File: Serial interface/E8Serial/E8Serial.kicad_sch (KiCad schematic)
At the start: 51 parts, among them J1 Conn_01x04_Male, J2 Conn_01x04_Male, J3 Conn_01x04_Male, J4 Conn_01x04_Male, Q1 BC548, Q2 BC548, Q3 BC548, SW1 NDB2, SW2 NDB1, SW3 PARITY ODD_EVEN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

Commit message: Schematic update 2024-04-14 plus fixes
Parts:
- removed U8: 74LS123, Package_DIP:DIP-16_W7.62mm, symbol E8Serial-rescue:74LS123-74xx
- added U8: (no value), Package_DIP:DIP-16_W7.62mm_Socket_LongPads, symbol DM series IC:DM9602
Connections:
- net +5V: now also U8.16 (VCC)
- net GND: now also U8.11 (A), U8.5 (A), U8.8 (GND)
- net SL: now also U8.7 (~{Q})
- net ~{RDA}: now also U8.9 (~{Q})
- net at U4.21 (XR): now also U5.12
- net at C5.1, R13.1: now also U8.1 (Cext)
- net at C5.2: now also U8.2 (RCext)
- net at U5.2: now also U8.4 (B)
- net at C6.2: now also U8.14 (RCext)
- net at C6.1, R14.1: now also U8.15 (Cext)
- new net: U8.12 (B), U8.6 (Q)
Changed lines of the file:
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@@
     (pin "1")
-  )
-  (symbol (lib_id "E8Serial-rescue:74LS123-74xx") (at 208.28 205.74 0) (unit 1)
-    (in_bom yes) (on_board yes)
-    (property "Reference" "U8" (id 0) (at 208.28 193.8782 0))
-    (property "Value" "74LS123" (id 1) (at 208.28 196.1896 0))
-    (property "Footprint" "Package_DIP:DIP-16_W7.62mm" (id 2) (at 208.28 205.74 0)
-      (effects (font (size 1.27 1.27)) hide)
-    )
-    (property "Datasheet" "http://www.ti.com/lit/gpn/sn74LS123" (id 3) (at 208.28 205.74 0)
-      (effects (font (size 1.27 1.27)) hide)
-    )
-    (pin "1")
-    (pin "13")
-    (pin "14")
-    (pin "15")
-    (pin "2")
-    (pin "3")
-    (pin "4")
-    (pin "10")
-    (pin "11")
-    (pin "12")
-    (pin "5")
-    (pin "6")
-    (pin "7")
-    (pin "9")
-    (pin "16")
-    (pin "8")
-  )
-  (symbol (lib_id "E8Serial-rescue:74LS123-74xx") (at 251.46 205.74 0) (unit 2)
-    (in_bom yes) (on_board yes)
-    (property "Reference" "U8" (id 0) (at 251.46 193.8782 0))
-    (property "Value" "74LS123" (id 1) (at 251.46 196.1896 0))
-    (property "Footprint" "Package_DIP:DIP-16_W7.62mm" (id 2) (at 251.46 205.74 0)
-      (effects (font (size 1.27 1.27)) hide)
-    )
-    (property "Datasheet" "http://www.ti.com/lit/gpn/sn74LS123" (id 3) (at 251.46 205.74 0)
-      (effects (font (size 1.27 1.27)) hide)
-    )
-    (pin "1")
-    (pin "13")
-    (pin "14")
-    (pin "15")
-    (pin "2")
-    (pin "3")
-    (pin "4")
-    (pin "10")
-    (pin "11")
-    (pin "12")
-    (pin "5")
-    (pin "6")
-    (pin "7")
-    (pin "9")
-    (pin "16")
-    (pin "8")
   )
   (symbol (lib_id "Device:R") (at 234.95 184.15 0) (mirror x) (unit 1)
@@
     (pin "4")
   )
-  (symbol (lib_id "E8Serial-rescue:74LS123-74xx") (at 27.94 260.35 0) (unit 3)
-    (in_bom yes) (on_board yes)
-    (property "Reference" "U8" (id 0) (at 33.782 259.1816 0)
-      (effects (font (size 1.27 1.27)) (justify left))
-    )
-    (property "Value" "74LS123" (id 1) (at 33.782 261.493 0)
-      (effects (font (size 1.27 1.27)) (justify left))
-    )
-    (property "Footprint" "" (id 2) (at 27.94 260.35 0)
-      (effects (font (size 1.27 1.27)) hide)
-    )
-    (property "Datasheet" "http://www.ti.com/lit/gpn/sn74LS123" (id 3) (at 27.94 260.35 0)
-      (effects (font (size 1.27 1.27)) hide)
-    )
-    (pin "1")
-    (pin "13")
-    (pin "14")
-    (pin "15")
-    (pin "2")
-    (pin "3")
-    (pin "4")
-    (pin "10")
-    (pin "11")
-    (pin "12")
-    (pin "5")
-    (pin "6")
-    (pin "7")
-    (pin "9")
-    (pin "16")
-    (pin "8")
-  )
   (symbol (lib_id "74xx:74LS04") (at 55.88 260.35 0) (unit 7)
     (in_bom yes) (on_board yes)
@@
     (pin "1")
   )
+  (symbol (lib_name "DM9602_1") (lib_id "DM series IC:DM9602") (at 251.46 205.74 0) (unit 2)
+    (in_bom yes) (on_board yes) (fields_autoplaced)
+    (property "Reference" "U8" (id 0) (at 251.46 194.4202 0))
+    (property "Value" "" (id 1) (at 251.46 196.9571 0))
+    (property "Footprint" "Package_DIP:DIP-16_W7.62mm_Socket_LongPads" (id 2) (at 251.46 205.74 0)
+      (effects (font (size 1.27 1.27)) hide)
+    )
+    (property "Datasheet" "http://www.ti.com/lit/gpn/sn74LS123" (id 3) (at 251.46 205.74 0)
+      (effects (font (size 1.27 1.27)) hide)
+    )
+    (pin "1")
+    (pin "2")
+    (pin "3")
+    (pin "4")
+    (pin "5")
+    (pin "6")
+    (pin "7")
+    (pin "10")
+    (pin "11")
+    (pin "12")
+    (pin "13")
+    (pin "14")
+    (pin "15")
+    (pin "9")
+    (pin "16")
+    (pin "8")
+  )
+  (symbol (lib_id "DM series IC:DM9602") (at 208.28 205.74 0) (unit 1)
+    (in_bom yes) (on_board yes) (fields_autoplaced)
+    (property "Reference" "U8" (id 0) (at 208.28 194.4202 0))
+    (property "Value" "" (id 1) (at 208.28 196.9571 0))
+    (property "Footprint" "" (id 2) (at 208.28 205.74 0)
+      (effects (font (size 1.27 1.27)) hide)
+    )
+    (property "Datasheet" "http://www.ti.com/lit/gpn/sn74LS123" (id 3) (at 208.28 205.74 0)
+      (effects (font (size 1.27 1.27)) hide)
+    )
+    (pin "1")
+    (pin "2")
+    (pin "3")
+    (pin "4")
+    (pin "5")
+    (pin "6")
+    (pin "7")
+    (pin "10")
+    (pin "11")
+    (pin "12")
+    (pin "12")
+    (pin "13")
+    (pin "14")
+    (pin "15")
+    (pin "16")
+    (pin "8")
+  )
+  (symbol (lib_id "DM series IC:DM9602") (at 27.94 260.35 0) (unit 3)
+    (in_bom yes) (on_board yes) (fields_autoplaced)
+    (property "Reference" "U8" (id 0) (at 33.782 259.5153 0)
+      (effects (font (size 1.27 1.27)) (justify left))
+    )
+    (property "Value" "" (id 1) (at 33.782 262.0522 0)
+      (effects (font (size 1.27 1.27)) (justify left))
+    )
+    (property "Footprint" "" (id 2) (at 27.94 260.35 0)
+      (effects (font (size 1.27 1.27)) hide)
+    )
+    (property "Datasheet" "http://www.ti.com/lit/gpn/sn74LS123" (id 3) (at 27.94 260.35 0)
+      (effects (font (size 1.27 1.27)) hide)
+    )
+    (pin "1")
+    (pin "2")
+    (pin "3")
+    (pin "4")
+    (pin "5")
+    (pin "6")
+    (pin "7")
+    (pin "10")
+    (pin "11")
+    (pin "12")
+    (pin "12")
+    (pin "13")
+    (pin "14")
+    (pin "15")
+    (pin "16")
+    (pin "8")
+  )
   (sheet_instances
     (path "/" (page "1"))
@@
       (reference "U7") (unit 1) (value "74LS165") (footprint "Package_DIP:DIP-16_W7.62mm")
     )
-    (path "/00000000-0000-0000-0000-000060e2db07"
-      (reference "U8") (unit 1) (value "74LS123") (footprint "Package_DIP:DIP-16_W7.62mm")
-    )
-    (path "/00000000-0000-0000-0000-000060e2f004"
-      (reference "U8") (unit 2) (value "74LS123") (footprint "Package_DIP:DIP-16_W7.62mm")
-    )
-    (path "/00000000-0000-0000-0000-00006143e14e"
-      (reference "U8") (unit 3) (value "74LS123") (footprint "")
-    )
-  )
+    (path "/89b31927-f663-4a3a-a530-c0fd8571c8d7"
+      (reference "U8") (unit 1) (value "DM9602") (footprint "Package_DIP:DIP-16_W7.62mm_Socket_LongPads")
+    )
+    (path "/1961fd7e-ea48-4fcd-9643-319fdbe0bda8"
+      (reference "U8") (unit 2) (value "DM9602") (footprint "Package_DIP:DIP-16_W7.62mm_Socket_LongPads")
+    )
+    (path "/a3990e5d-c3b4-40a6-9c0e-38537b9470eb"
+      (reference "U8") (unit 3) (value "DM9602") (footprint "Package_DIP:DIP-16_W7.62mm_Socket_LongPads")
+    )
+  )

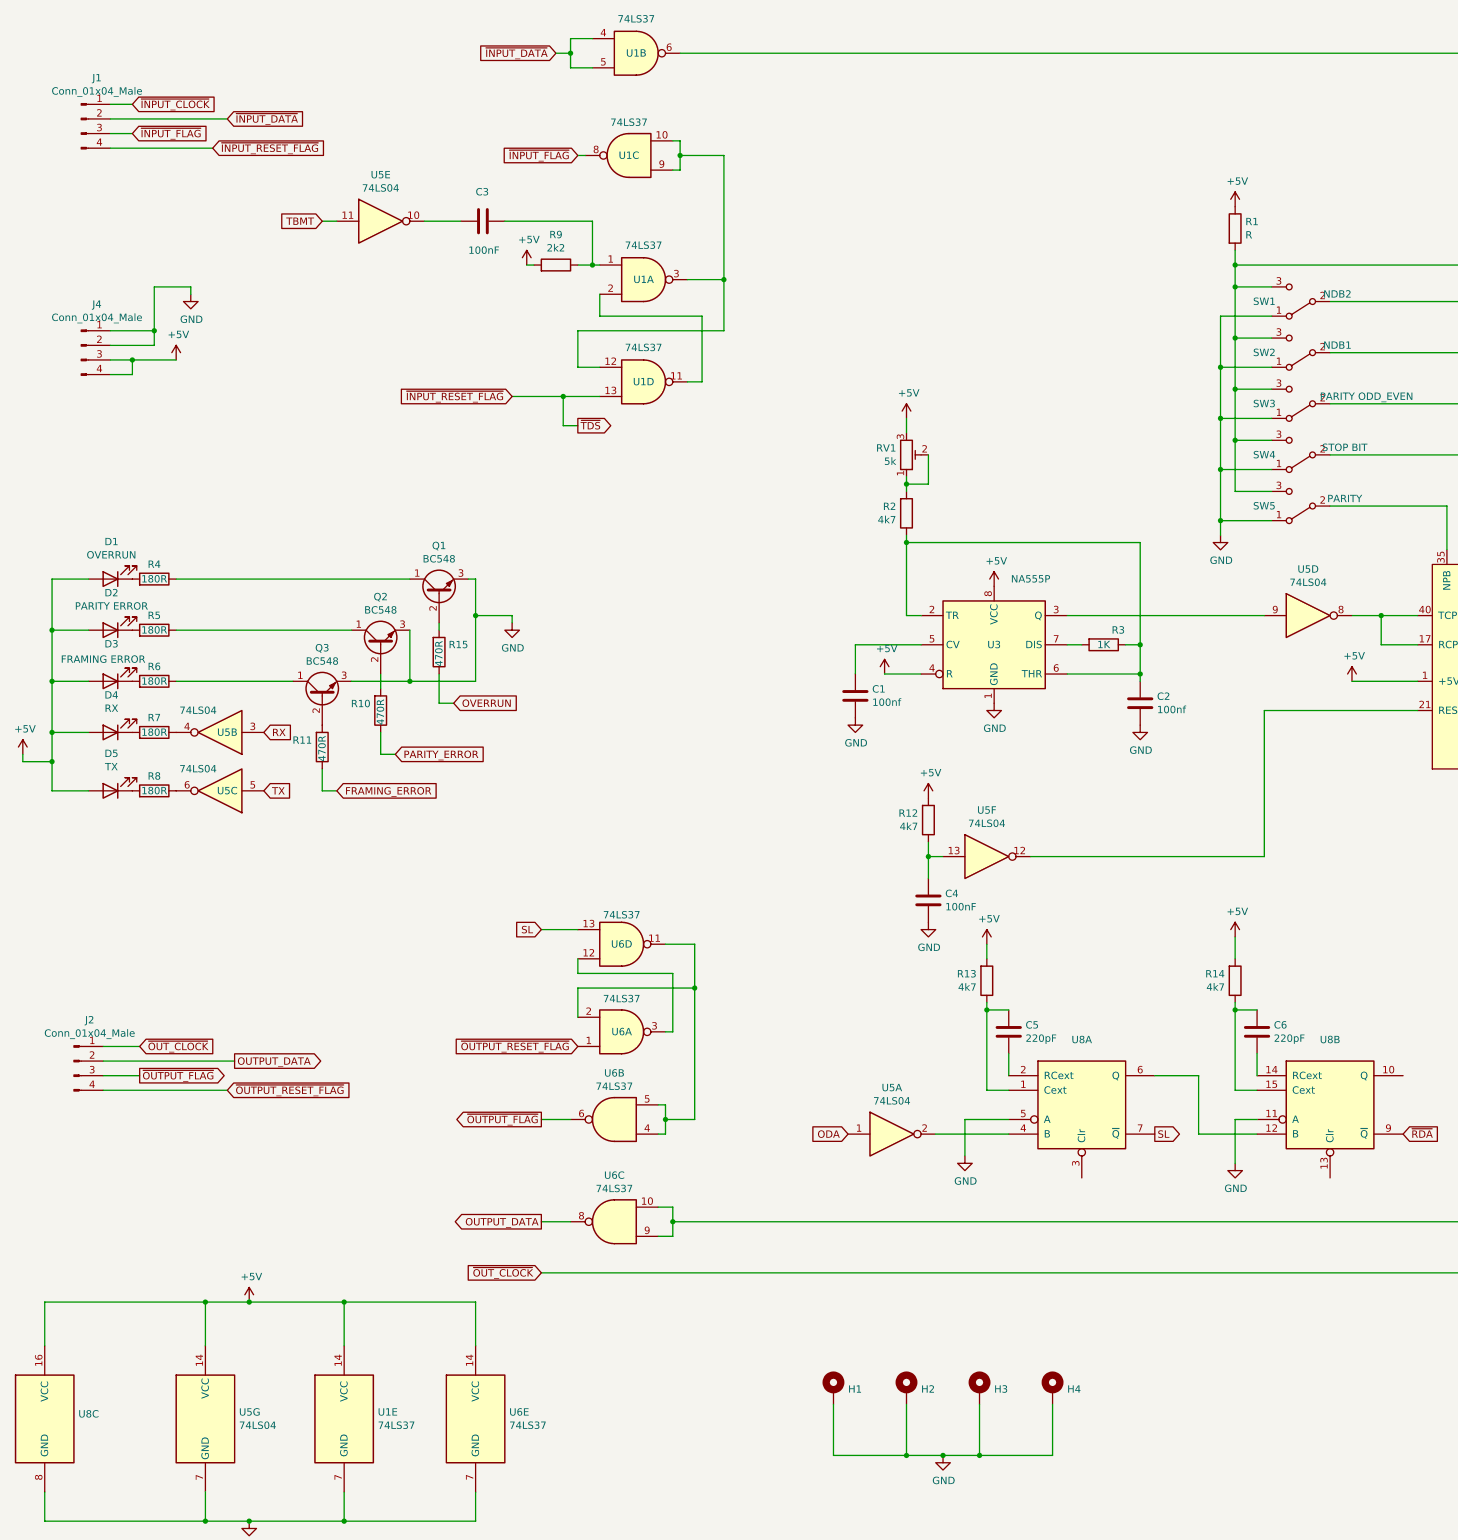
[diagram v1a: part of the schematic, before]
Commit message: Changes 20-7-2025 E8/T. Connected 3 missing supply rail tracks to ICS Added flood fill top and bottom to reduce noise E8/F Corrected labelling on RHS board to reflect EXT_LA not GND Changed fast slow switch operation so fast is in the DOWN position. E8/C. Ran a new track to the 2 pin JST connector from EXT_LA from 10 pin connector on SR input. Added files for E8MX, 2k byte memory expansion board
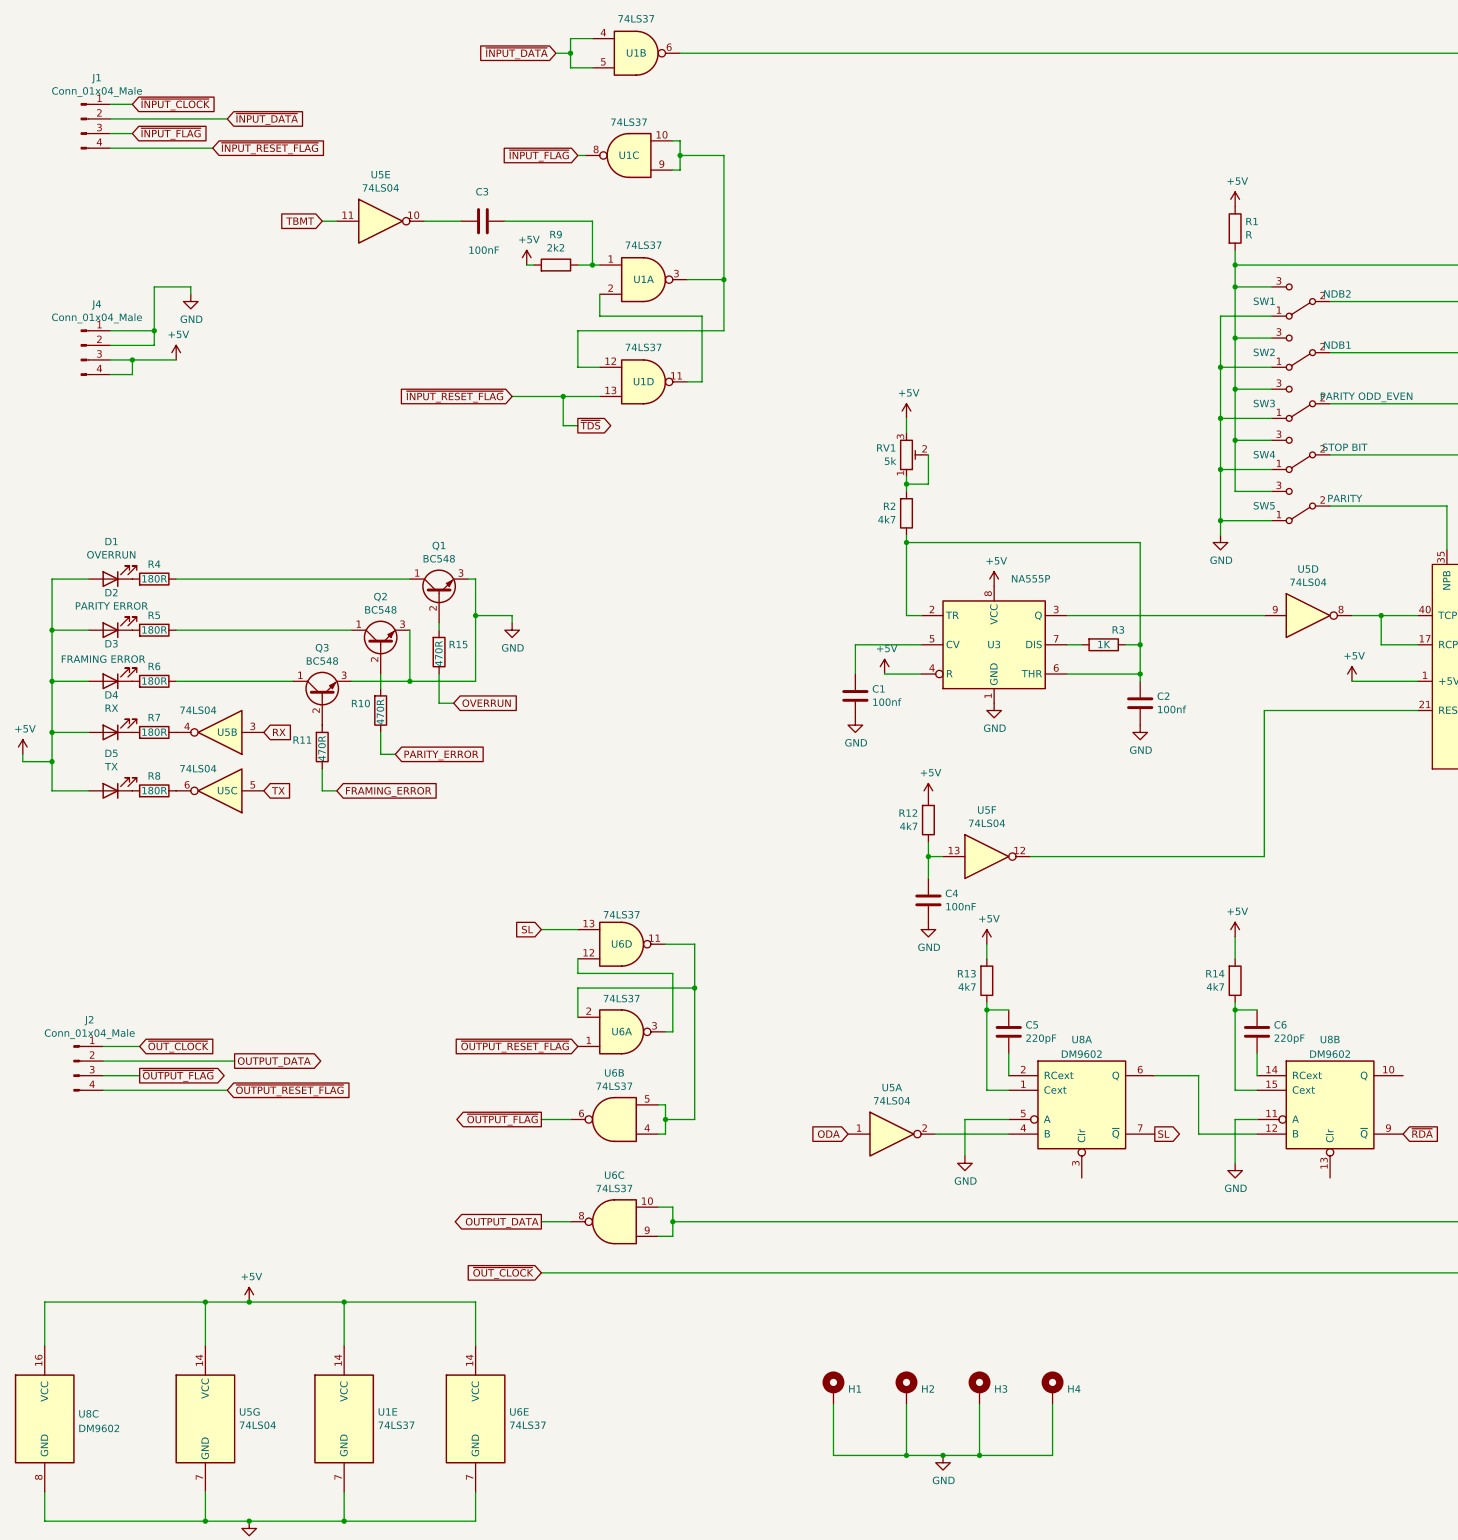
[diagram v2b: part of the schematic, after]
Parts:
- SW3: value PARITY ODD_EVEN -> PARITY ODD_EVEN
- SW5: value PARITY -> PARITY
- U8: value (none) -> DM9602
- U8: value (none) -> DM9602; footprint (none) -> Package_DIP:DIP-16_W7.62mm_Socket_LongPads
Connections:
- net at U4.21 (RESET): now also U5.12
